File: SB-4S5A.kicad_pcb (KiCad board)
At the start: 2 copper layers, 130 x 60 mm, 0 parts

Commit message: Some updates, net-ties and such.
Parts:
- added C1: 0.1u, Capacitors_SMD:C_0402, F.Cu at (137.7, 88.7)
- added C2: 0.1u, Capacitors_SMD:C_0402, F.Cu at (151.6, 82.6)
- added C3: 0.1u, Capacitors_SMD:C_0402, F.Cu at (160.1, 71.9)
- added C4: 0.1u, Capacitors_SMD:C_0402, F.Cu at (163.7, 67.1)
- added C5: 0.1u, Capacitors_SMD:C_0402, F.Cu at (141.6, 88.7)
- added C6: 2.2u, Capacitors_SMD:C_0402, F.Cu at (147.5, 83.6)
- added D1: BAT54HT1G, Diodes_SMD:D_SOD-323, F.Cu at (148.8, 62.8)
- added J1: I2C, Connectors:Grove_1x04, F.Cu at (118.7, 78.8)
- added J2: BATIO, Connectors:Grove_1x04, F.Cu at (118.7, 65.0)
- added Q1: CSD17308Q3, Housings_SON:VSON-8_3.3x3.3mm_Pitch0.65mm_NexFET, F.Cu at (139.2, 57.0)
- added Q2: CSD17308Q3, Housings_SON:VSON-8_3.3x3.3mm_Pitch0.65mm_NexFET, F.Cu at (132.0, 57.0)
- added Q3: 2N7002, TO_SOT_Packages_SMD:SOT-23, F.Cu at (134.6, 80.3)
- added R1: 100R, Resistors_SMD:R_0402, F.Cu at (152.5, 68.1)
- added R10: 100R, Resistors_SMD:R_0402, F.Cu at (152.5, 73.0)
- added R11: 10M, Resistors_SMD:R_0402, F.Cu at (156.5, 67.2)
- added R12: 5.1K, Resistors_SMD:R_0402, F.Cu at (147.7, 78.8)
- added R13: 10K, Resistors_SMD:R_0402, F.Cu at (163.8, 62.3)
- added R14: 10K, Resistors_SMD:R_0402, F.Cu at (143.9, 83.7)
- added R15: 100R, Resistors_SMD:R_0402, F.Cu at (155.5, 62.3)
- added R16: 100R, Resistors_SMD:R_0402, F.Cu at (147.8, 74.0)
- added R17: NET-TIE, Oddities:NetTie-I_Connected, F.Cu at (137.5, 71.7)
- added R18: NET-TIE, Oddities:NetTie-I_Connected, F.Cu at (127.7, 80.1)
- added R2: 100R, Resistors_SMD:R_0402, F.Cu at (143.4, 74.0)
- added R3: 100R, Resistors_SMD:R_0402, F.Cu at (140.0, 79.1)
- added R4: 100R, Resistors_SMD:R_0402, F.Cu at (133.6, 86.2)
- added R5: 100R, Resistors_SMD:R_0402, F.Cu at (126.2, 87.6)
- added R6: 0.001R, Resistors_SMD:R_1206, F.Cu at (147.4, 68.6)
- added R7: 100R, Resistors_SMD:R_0402, F.Cu at (159.9, 62.3)
- added R8: 10M, Resistors_SMD:R_0402, F.Cu at (144.0, 78.8)
- added R9: 5.1K, Resistors_SMD:R_0402, F.Cu at (139.7, 84.0)
- added TH1: 10K, Resistors_SMD:R_0402, F.Cu at (151.7, 77.8)
- added TH2: 10K, Resistors_SMD:R_0402, F.Cu at (167.3, 62.3)
- added TH3: 10K, Resistors_SMD:R_0402, F.Cu at (156.4, 72.0)
- added TH4: 10K, Resistors_SMD:R_0402, F.Cu at (160.0, 67.2)
- added U1: bq40z50-r2, TI SBS:QFN-32_EP_3.8x3.8_Pitch0.4mm, F.Cu at (128.8, 71.8)

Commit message: Added battery footprint
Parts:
- added BT1: 3.7v, TI SBS:105070, F.Cu at (95.3, 90.0)
- added BT2: 3.7v, TI SBS:105070, F.Cu at (155.0, 90.0)
- added BT3: 3.7v, TI SBS:105070, B.Cu at (155.0, 90.0)
- added BT4: 3.7v, TI SBS:105070, B.Cu at (95.0, 90.0)
- R1: value 100R -> NET-TIE; footprint Resistors_SMD:R_0402 -> Oddities:NetTie-I_Connected
- R10: value 100R -> 10M
- R11: value 10M -> 5.1K
- R12: value 5.1K -> 100R
- R13: value 10K -> 10M
- R14: value 10K -> 5.1K
- R15, R16: value 100R -> 10K
- R17, R18: value NET-TIE -> 100R; footprint Oddities:NetTie-I_Connected -> Resistors_SMD:R_0402
- R6: value 0.001R -> 100R; footprint Resistors_SMD:R_1206 -> Resistors_SMD:R_0402
- R7: value 100R -> 0.001R; footprint Resistors_SMD:R_0402 -> Resistors_SMD:R_1206
- R8: value 10M -> 100R
- R9: value 5.1K -> NET-TIE; footprint Resistors_SMD:R_0402 -> Oddities:NetTie-I_Connected
- moved R9 64.0 mm to (151.5, 21.1)
- moved C1 63.4 mm to (156.5, 28.2)
- moved J1 58.6 mm to (133.0, 22.0)
- moved C2 58.0 mm to (101.3, 53.7)
- moved C5 57.7 mm to (154.4, 32.5)
- moved R5 56.4 mm to (142.2, 33.5)
- moved R4 56.2 mm to (150.7, 32.6)
- moved R10 56.1 mm to (101.6, 49.4)
- moved R6 50.2 mm to (157.0, 19.4)
- moved C6 46.7 mm to (150.0, 36.9)
- moved R12 45.3 mm to (146.2, 33.5)
- moved R11 43.4 mm to (156.8, 23.8)
- moved TH4 41.7 mm to (122.5, 48.8)
- moved J2 40.1 mm to (122.0, 25.0)
- moved R14 38.8 mm to (129.8, 47.5)
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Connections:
- R1 pad 1: Net-(BT1-Pad1) -> GND
- R1 pad 2: Net-(C1-Pad1) -> GNDD
- R10 pad 1: Net-(R10-Pad1) -> Net-(Q1-Pad4)
- R10 pad 2: Net-(Q1-Pad5) -> Net-(BT1-Pad1)
- R11 pad 1: Net-(Q2-Pad4) -> Net-(R11-Pad1)
- R11 pad 2: PACK+ -> Net-(Q1-Pad4)
- R12 pad 2: Net-(Q2-Pad4) -> Net-(Q1-Pad5)
- R13 pad 1: Net-(Q3-Pad1) -> Net-(Q2-Pad4)
- R13 pad 2: GNDS -> PACK+
- R14 pad 1: PACK+ -> Net-(R14-Pad1)
- R14 pad 2: Net-(R14-Pad2) -> Net-(Q2-Pad4)
- R15 pad 1: Net-(R15-Pad1) -> Net-(Q3-Pad1)
- R15 pad 2: Net-(J1-Pad1) -> GNDS
- R16 pad 1: Net-(R16-Pad1) -> PACK+
- R16 pad 2: Net-(J1-Pad2) -> Net-(R16-Pad2)
- R17 pad 1: GND -> Net-(R17-Pad1)
- R17 pad 2: GNDD -> Net-(J1-Pad1)
- R18 pad 1: PACK- -> Net-(R18-Pad1)
- R18 pad 2: GNDS -> Net-(J1-Pad2)
- R2 pad 1: Net-(BT1-Pad2) (its old number) -> Net-(BT1-Pad1)
- R2 pad 2: Net-(C1-Pad2) -> Net-(C1-Pad1)
- R3 pad 2: Net-(C2-Pad2) -> Net-(C1-Pad2)
- R4 pad 2: Net-(C3-Pad2) -> Net-(C2-Pad2)
- R5 pad 1: GND -> Net-(BT3-Pad2)
- R5 pad 2: Net-(C5-Pad2) -> Net-(C3-Pad2)
- R6 pad 1: PACK- -> GND
- R6 pad 2: GND -> Net-(C5-Pad2)
- R7 pad 2: Net-(C5-Pad1) -> GND
- R8 pad 1: Net-(Q1-Pad4) -> PACK-
- R8 pad 2: Net-(BT1-Pad1) -> Net-(C5-Pad1)
- R9 pad 1: Net-(R9-Pad1) -> PACK-
- R9 pad 2: Net-(Q1-Pad4) -> GNDS
- U1 pad 18: Net-(R16-Pad1) -> Net-(R18-Pad1)
- U1 pad 19: Net-(R15-Pad1) -> Net-(R17-Pad1)
- U1 pad 26: Net-(R10-Pad1) -> Net-(R12-Pad1)
- U1 pad 27: Net-(R14-Pad2) -> Net-(R16-Pad2)
- U1 pad 28: Net-(R12-Pad1) -> Net-(R14-Pad1)
- U1 pad 31: Net-(R9-Pad1) -> Net-(R11-Pad1)
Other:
- board outline removed
- copper layers 2 -> 4
- net class Default: clearance 0.2 -> 0; trace_width 0.25 -> 0.2
- net class PWR added: clearance 0, trace_width 5, via_dia 0.8, via_drill 0.4
- rule pad_to_mask_clearance: 0.2 -> 0
- rule trace_clearance: 0.2 -> 0

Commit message: Started board layout.
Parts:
- R7, TH4: moved to B.Cu
- moved Q1 87.6 mm to (75.0, 76.0), turned to 90 degrees
- moved R9 81.8 mm to (90.0, 75.0)
- moved R6 76.4 mm to (118.0, 85.0)
- moved R13 72.3 mm to (74.0, 63.0)
- moved R11 65.0 mm to (126.0, 81.0)
- moved Q2 62.2 mm to (75.0, 70.0), turned to 270 degrees
- moved C5 57.4 mm to (117.0, 76.0)
- moved Q3 55.5 mm to (82.0, 68.0), turned to 90 degrees
- moved R14 53.1 mm to (79.0, 63.0)
- moved J2 49.2 mm to (92.0, 64.0), turned to 90 degrees
- moved J1 48.9 mm to (108.0, 64.0), turned to 90 degrees
- moved TH4 47.3 mm to (96.0, 88.0)
- moved C6 45.5 mm to (121.0, 72.0)
- moved R1 44.5 mm to (91.0, 71.0)
- moved R10 42.9 mm to (75.0, 83.0)
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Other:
- board outline added: 110 x 30 mm

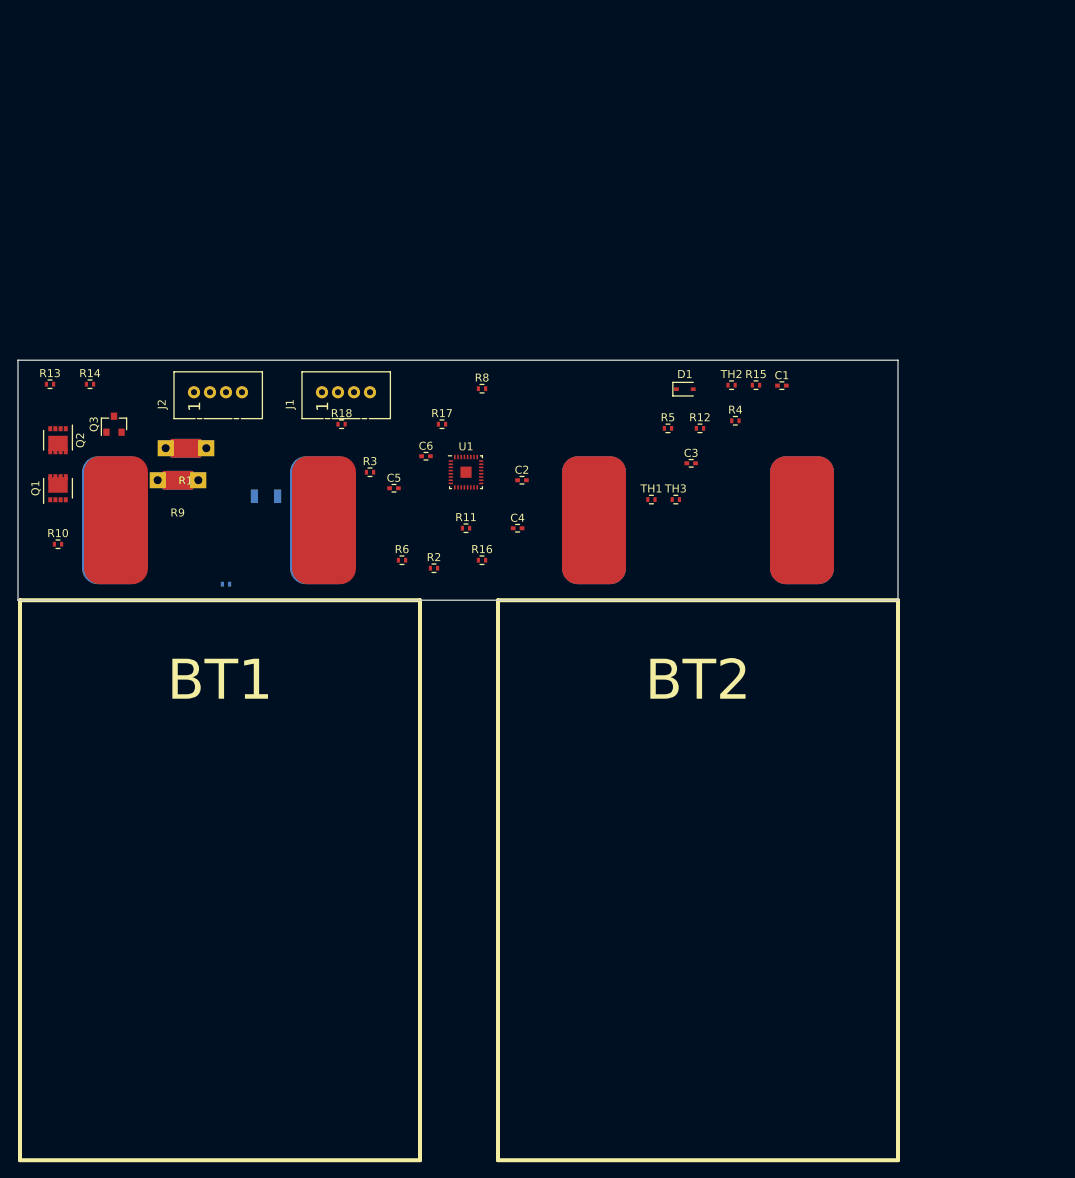
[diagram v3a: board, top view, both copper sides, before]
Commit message: Add simple battery 3d model, more layout.
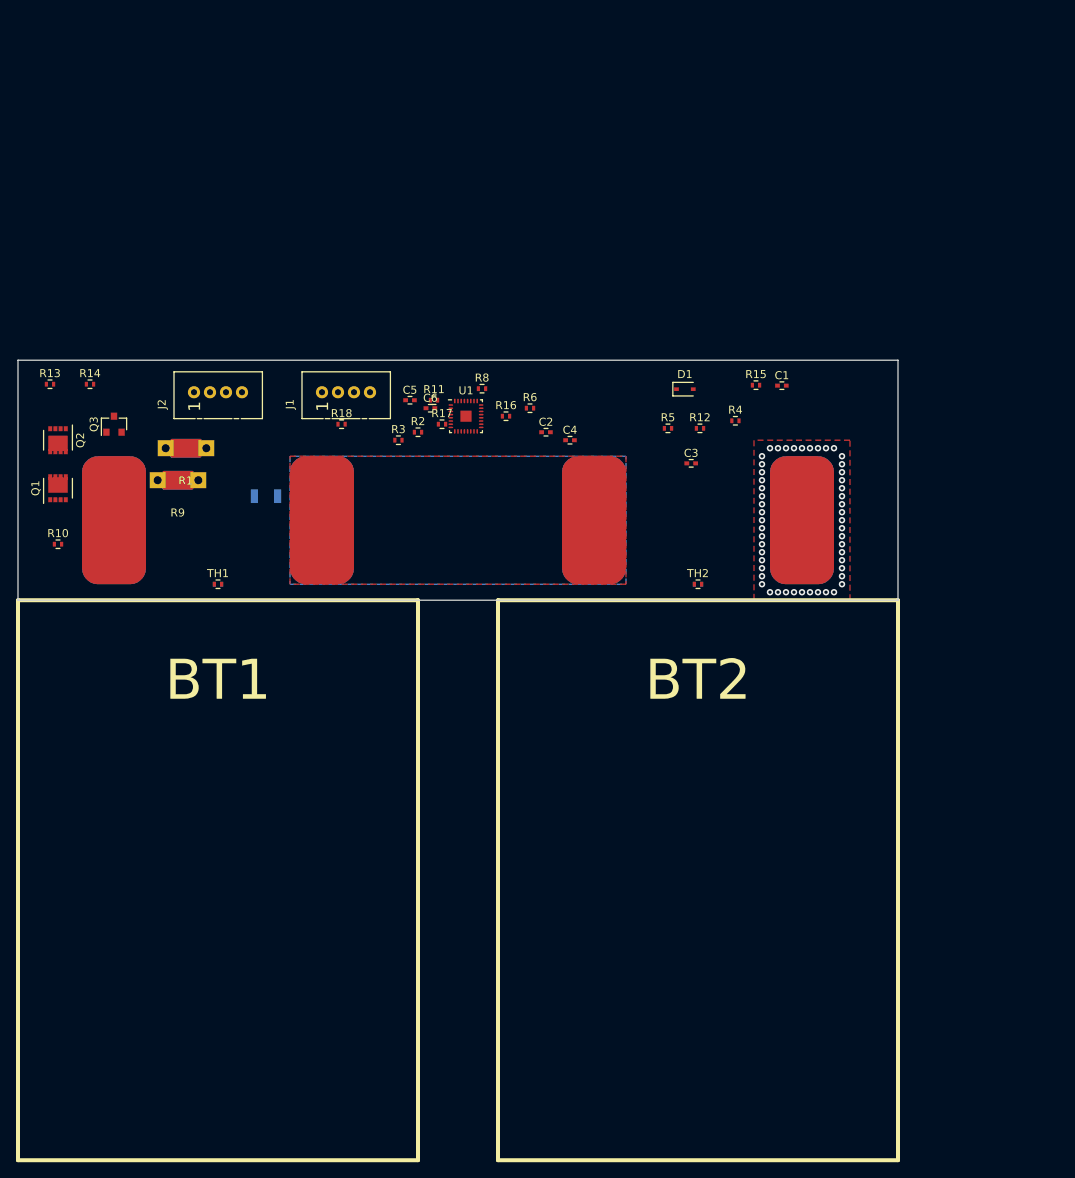
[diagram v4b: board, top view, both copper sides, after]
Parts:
- TH3: moved to B.Cu
- moved TH1 55.2 mm to (95.0, 88.0)
- moved TH2 25.2 mm to (155.0, 88.0)
- moved R6 24.8 mm to (134.0, 66.0)
- moved R16 18.2 mm to (131.0, 67.0)
- moved R2 17.1 mm to (120.0, 69.0)
- moved R11 16.5 mm to (122.0, 65.0)
- moved C4 12.8 mm to (139.0, 70.0)
- moved C5 11.2 mm to (119.0, 65.0)
- moved TH3 10.9 mm to (155.0, 88.0)
- moved U1 7.00 mm to (126.0, 67.0)
- moved C2 6.71 mm to (136.0, 69.0)
- moved C6 6.03 mm to (121.5, 66.0)
- moved R3 5.35 mm to (117.5, 70.0)
- moved TH4 1.00 mm to (95.0, 88.0)
- moved BT1 0.25 mm to (95.0, 90.0)
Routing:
- net Net-(BT2-Pad2): vias 0 -> 52
- added copper zone on F.Cu, net Net-(BT1-Pad2)
- added copper zone on F.Cu, net Net-(BT2-Pad2)
- added copper zone on B.Cu, net Net-(BT3-Pad2)

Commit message: Finish place and routing.
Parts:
- removed J2: BATIO, Connectors:Grove_1x04
- removed R9: NET-TIE, Oddities:NetTie-I_Connected
- added R19: 100R, Resistors_SMD:R_0402, F.Cu at (95.2, 68.5)
- added R20: 100R, Resistors_SMD:R_0402, F.Cu at (94.0, 68.5)
- J1: value I2C -> CONN_01X06; footprint Connectors:Grove_1x04 -> TI SBS:14110613002XXX
- R1: footprint Oddities:NetTie-I_Connected -> Resistors_SMD:R_0402
- R7: moved to F.Cu
- moved R15 86.5 mm to (75.8, 62.2)
- moved R12 79.6 mm to (75.8, 72.5), turned to 180 degrees
- moved C1 64.0 mm to (102.2, 72.8), turned to 180 degrees
- moved R4 61.3 mm to (98.5, 71.2), turned to 270 degrees
- moved C3 56.1 mm to (98.1, 72.8), turned to 180 degrees
- moved R16 55.3 mm to (75.8, 64.8)
- moved R5 54.1 mm to (97.2, 71.2), turned to 270 degrees
- moved D1 50.6 mm to (103.2, 70.8), turned to 180 degrees
- moved R11 45.7 mm to (77.2, 74.2), turned to 270 degrees
- moved R6 44.9 mm to (89.7, 73.6)
- moved C4 43.1 mm to (96.0, 72.8), turned to 180 degrees
- moved R8 39.3 mm to (89.7, 72.4)
- moved C2 36.0 mm to (100.2, 72.8), turned to 180 degrees
- moved U1 31.6 mm to (98.0, 81.8), turned to 270 degrees
- moved R17 30.3 mm to (92.8, 68.5), turned to 90 degrees
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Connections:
- net Net-(BT1-Pad1) renamed /BAT+
- net Net-(BT1-Pad2) renamed /VC3A
- net Net-(BT2-Pad2) renamed /VC2A
- net Net-(BT3-Pad2) renamed /VC1A
- net Net-(C1-Pad1) renamed /VC4
- net Net-(C1-Pad2) renamed /VC3
- net Net-(C2-Pad2) renamed /VC2
- net Net-(C3-Pad2) renamed /VC1
- net Net-(C5-Pad1) renamed /SRN
- net Net-(C5-Pad2) renamed /SRP
- net Net-(C6-Pad1) renamed /PBI
- net Net-(D1-Pad1) renamed /BAT
- net Net-(Q1-Pad4) renamed /CHG_G
- net Net-(Q1-Pad5) renamed /MID
- net Net-(Q2-Pad4) renamed /DSG_G
- net Net-(R11-Pad1) renamed /CHG
- net Net-(R12-Pad1) renamed /_VCC_
- net Net-(R14-Pad1) renamed /DSG
- net Net-(R16-Pad2) renamed /PACK
- BT4 pad 2: GND -> /BAT-
- C4 pad 2: GND -> GNDD
- J1 pad 1: Net-(J1-Pad1) -> /BTP_INT
- J1 pad 2: Net-(J1-Pad2) -> /~PRES~
- J1 pad 3: Net-(J1-Pad3) -> /SMBD
- J1 pad 4: GNDS -> /SMBC
- R1 pad 1: GND -> /BAT-
- R15 pad 2: GNDS -> PACK-
- R17 pad 1: Net-(R17-Pad1) -> /SMBD_
- R17 pad 2: Net-(J1-Pad1) -> /SMBD
- R18 pad 1: Net-(R18-Pad1) -> /SMBC_
- R18 pad 2: Net-(J1-Pad2) -> /SMBC
- R6 pad 1: GND -> /BAT-
- R7 pad 2: GND -> /BAT-
- U1 pad 15: Net-(J2-Pad1) -> /BTP_INT_
- U1 pad 16: Net-(J2-Pad2) -> /~PRES/SHDN~_
- U1 pad 18: Net-(R18-Pad1) -> /SMBD_
- U1 pad 19: Net-(R17-Pad1) -> /SMBC_
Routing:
- net /VC2A: track 0.00 -> 75.5 mm, vias 52 -> 0
- net Net-(TH2-Pad1): track 0.00 -> 70.0 mm, vias 0 -> 2
- net Net-(TH3-Pad1): track 0.00 -> 67.4 mm, vias 0 -> 2
- net /DSG: track 0.00 -> 65.8 mm, vias 0 -> 2
- net /PACK: track 0.00 -> 55.6 mm, vias 0 -> 2
- net /CHG: track 0.00 -> 45.5 mm, vias 0 -> 2
- net /_VCC_: track 0.00 -> 43.1 mm, vias 0 -> 2
- net /BAT+: track 0.00 -> 31.5 mm, vias 0 -> 2
- net /SMBC_: track 0.00 -> 24.9 mm, vias 0 -> 2
- net /SMBD_: track 0.00 -> 24.1 mm, vias 0 -> 2
- net /BTP_INT_: track 0.00 -> 24.0 mm, vias 0 -> 2
- net /~PRES/SHDN~_: track 0.00 -> 23.9 mm, vias 0 -> 2
- net /VC1A: track 0.00 -> 19.4 mm, vias 0 -> 1
- net /VC3A: track 0.00 -> 19.2 mm
- net PACK-: track 0.00 -> 17.6 mm
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- added copper zone on F.Cu, net /BAT+
- added copper zone on B.Cu, net /BAT-
- added copper zone on F.Cu, net /BAT-
- added copper zone on F.Cu, net /MID
- added copper zone on B.Cu, net /VC2A
- added copper zone on F.Cu, net GNDD
- added copper zone on In1.Cu, net GNDD
- added copper zone on F.Cu, net PACK+
- added copper zone on F.Cu, net PACK-
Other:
- net class Default: clearance 0 -> 0.16
- net class PWR: clearance 0 -> 0.16
- rule trace_clearance: 0 -> 0.16
